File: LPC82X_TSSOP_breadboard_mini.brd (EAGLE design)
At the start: 26 x 15.9 mm, 16 parts, among them Q1 12MHz

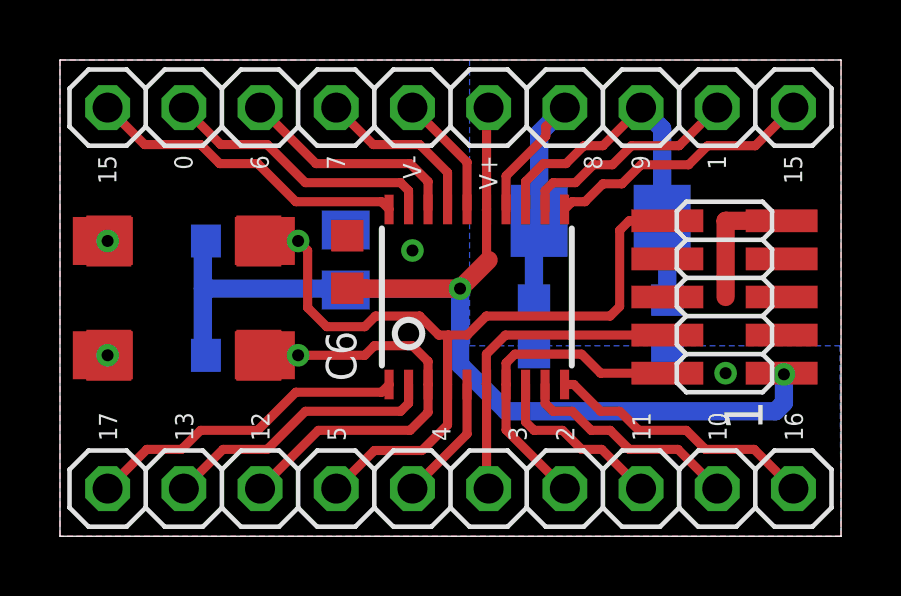
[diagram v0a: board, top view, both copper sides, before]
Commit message: * started with lpc824 TSSOP breakout
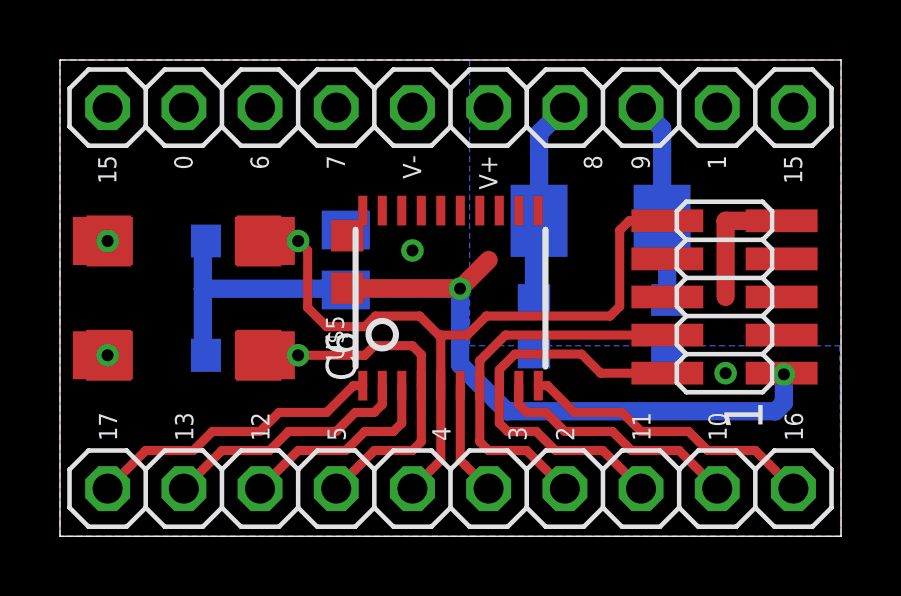
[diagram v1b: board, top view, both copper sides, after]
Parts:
- removed LPC812: LPC812M101JDH20, LPC800:TSSOP20
- added U$5: LPC82XM101JDH20, LPC800:TSSOP20
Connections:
- removed net PIO0_16: JP1.10, LPC812.10
- removed net PIO0_6: JP2.8, LPC812.18
- removed net PIO0_7: JP2.7, LPC812.17
- new net PIO0_23: JP1.1, U$5.1
- new net VREFN: JP2.7, U$5.17
- new net VREF_P: JP2.8, U$5.18
- net PIO0_0: now also U$5.19; no longer LPC812.19
- net PIO0_1: now also U$5.12; no longer LPC812.12
- net PIO0_10: now also JP1.10, U$5.10; no longer JP1.9, LPC812.9
- net PIO0_11: now also JP1.9, U$5.9; no longer JP1.8, LPC812.8
- net PIO0_12: now also JP1.4, U$5.4; no longer JP1.3, LPC812.3
- net PIO0_13: now also JP1.3, U$5.3; no longer JP1.2, LPC812.2
- net PIO0_14: now also U$5.20; no longer LPC812.20
- net PIO0_15: now also U$5.11; no longer LPC812.11
- net PIO0_17: now also JP1.2, U$5.2; no longer JP1.1, LPC812.1
- net PIO0_2: now also JP1.8, U$5.8; no longer JP1.7, LPC812.7
- net PIO0_3: now also JP1.7, U$5.7; no longer JP1.6, LPC812.6
- net PIO0_4: now also JP1.6, U$5.6; no longer JP1.5, LPC812.5
- net PIO0_5: now also JP1.5, U$5.5; no longer JP1.4, LPC812.4
- net PIO0_8: now also U$5.14; no longer LPC812.14
- net PIO0_9: now also U$5.13; no longer LPC812.13
- net VDD: now also U$5.15; no longer LPC812.15
- net VSS: now also U$5.16; no longer LPC812.16
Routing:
- net PIO0_14: track 10.8 -> 0.00 mm
- net PIO0_23: track 0.00 -> 9.93 mm
- net PIO0_0: track 9.26 -> 0.00 mm
- net PIO0_16: track 9.07 -> 0.00 mm
- net PIO0_15: track 9.04 -> 0.00 mm
- net PIO0_6: track 7.55 -> 0.00 mm
- net PIO0_1: track 7.51 -> 0.00 mm
- net PIO0_7: track 5.84 -> 0.00 mm
- net PIO0_9: track 13.5 -> 7.66 mm
- net VDD: track 38.5 -> 33.5 mm
- net PIO0_8: track 11.9 -> 7.73 mm
- net VSS: track 8.56 -> 4.41 mm
- net PIO0_2: track 10.8 -> 13.5 mm
- net PIO0_17: track 10.8 -> 8.40 mm
- net PIO0_13: track 9.30 -> 6.88 mm
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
